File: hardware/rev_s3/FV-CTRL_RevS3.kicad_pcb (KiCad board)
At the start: 2 copper layers, 100 x 100 mm, 69 parts, among them J1 12V INPUT, J10 LIMIT SWITCHES, J11 DROP SENSOR COL 1, J12 DROP SENSOR COL 2, J2 XL4015 A, J21 USB_C_16P, J3 XL4015 B, J4 5V R-78E5.0-1.0, J5 S1_TOP, J6 S1_BOT, J7 S2_TOP, J8 S2_BOT, J9 I2C SPARE, SW1 RESET, SW2 BOOT, U1 ESP32-S3-WROOM-1U, U3 LD1117S33

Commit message: fix: reinforce RevS3 servo B supply route
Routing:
- net +6V_B: track 145.7 -> 223.0 mm
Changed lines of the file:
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@@
+	)
+	(segment
+		(start 198 175.54)
+		(end 198 185.54)
+		(width 1.2)
+		(layer "F.Cu")
+		(net "+6V_B")
 	)
 	(segment
@@
 	)
 	(segment
+		(start 198 185.54)
+		(end 194 185.54)
+		(width 1.2)
+		(layer "F.Cu")
+		(net "+6V_B")
+	)
+	(segment
 		(start 121.6 189.9)
 		(end 121.75 189.9)
@@
 	)
 	(segment
+		(start 198 175.54)
+		(end 194 175.54)
+		(width 1.2)
+		(layer "F.Cu")
+		(net "+6V_B")
+	)
+	(segment
 		(start 183.15 144.5)
 		(end 183.15 144.6)
@@
 	)
 	(segment
+		(start 198 126.2)
+		(end 198 175.54)
+		(width 1.2)
+		(layer "F.Cu")
+		(net "+6V_B")
+	)
+	(segment
 		(start 186.75 130.949999)
 		(end 186.7 131)
@@
 		(layer "F.Cu")
 		(net "+6V_B")
+	)
+	(segment
+		(start 188.1 126.2)
+		(end 198 126.2)
+		(width 1.2)
+		(layer "F.Cu")
+		(net "+6V_B")

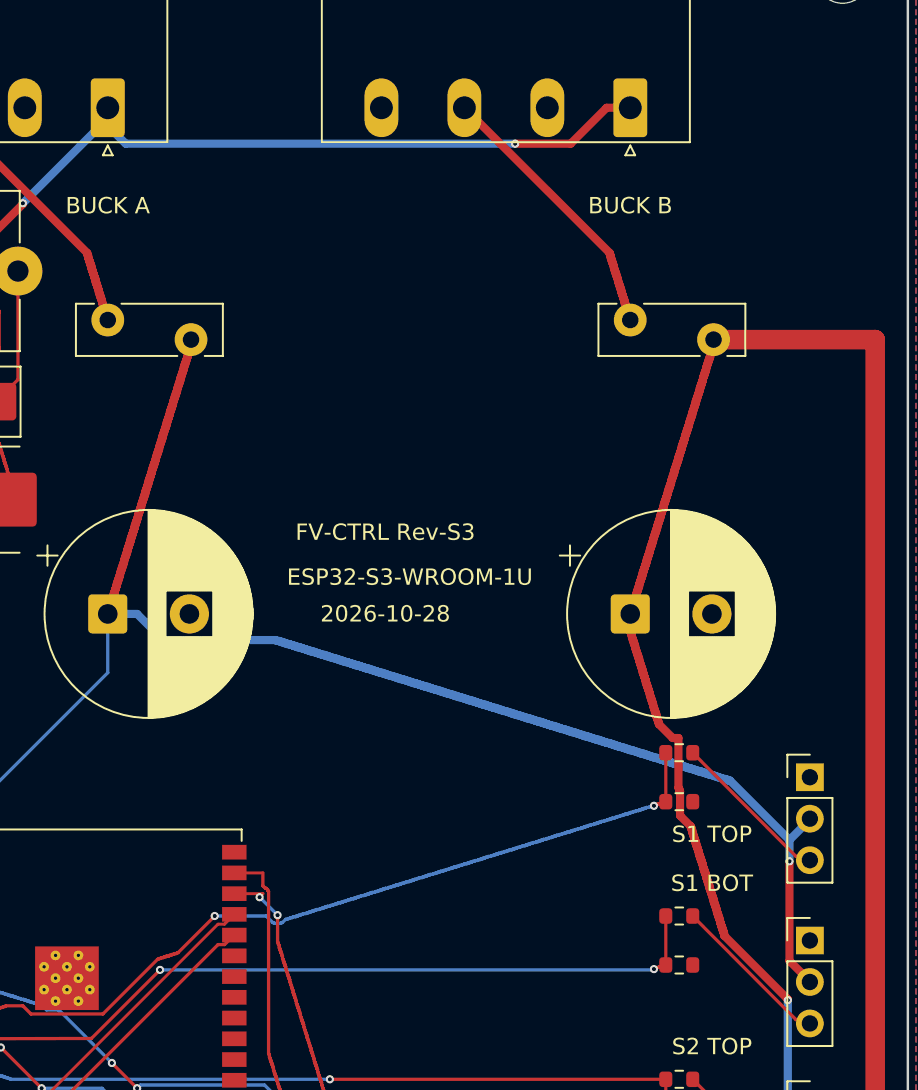
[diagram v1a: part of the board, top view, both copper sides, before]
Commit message: fix: reinforce RevS3 servo A and shared 12V routes
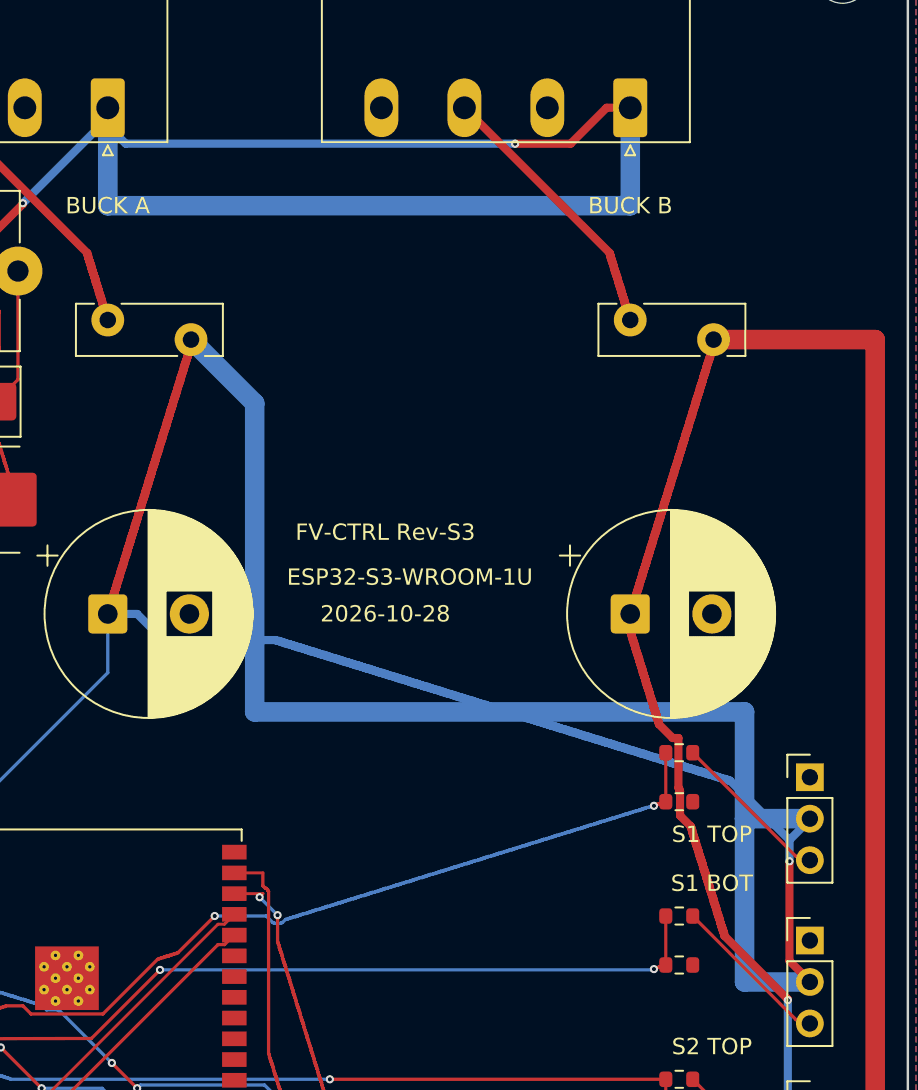
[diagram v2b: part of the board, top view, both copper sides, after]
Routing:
- net +6V_A: track 137.8 -> 216.8 mm
- net +12V: track 148.8 -> 192.8 mm
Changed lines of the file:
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@@
 	)
 	(segment
+		(start 151 118)
+		(end 183 118)
+		(width 1.2)
+		(layer "B.Cu")
+		(net "+12V")
+	)
+	(segment
+		(start 183 118)
+		(end 183 112)
+		(width 1.2)
+		(layer "B.Cu")
+		(net "+12V")
+	)
+	(segment
 		(start 119.6 145.75)
 		(end 117.2 143.35)
@@
 	)
 	(segment
+		(start 151 112)
+		(end 151 118)
+		(width 1.2)
+		(layer "B.Cu")
+		(net "+12V")
+	)
+	(segment
 		(start 145.8 117.85)
 		(end 150.7 112.95)
@@
 	)
 	(segment
+		(start 190 149)
+		(end 190 155.54)
+		(width 1.2)
+		(layer "B.Cu")
+		(net "+6V_A")
+	)
+	(segment
 		(start 168.25 146.75)
 		(end 168.15 146.75)
@@
 	)
 	(segment
+		(start 160 149)
+		(end 190 149)
+		(width 1.2)
+		(layer "B.Cu")
+		(net "+6V_A")
+	)
+	(segment
 		(start 162.15 144.85)
 		(end 162 144.85)
@@
 	)
 	(segment
+		(start 156.1 126.2)
+		(end 160 130.1)
+		(width 1.2)
+		(layer "B.Cu")
+		(net "+6V_A")
+	)
+	(segment
 		(start 186.1 152.3)
 		(end 186.05 152.25)
@@
 	)
 	(segment
+		(start 160 130.1)
+		(end 160 149)
+		(width 1.2)
+		(layer "B.Cu")
+		(net "+6V_A")
+	)
+	(segment
 		(start 167 146.35)
 		(end 166.85 146.35)
@@
 	)
 	(segment
+		(start 190 155.54)
+		(end 190 165.54)
+		(width 1.2)
+		(layer "B.Cu")
+		(net "+6V_A")
+	)
+	(segment
 		(start 181.7 150.9)
 		(end 181.55 150.9)
@@
 	)
 	(segment
+		(start 190 155.54)
+		(end 194 155.54)
+		(width 1.2)
+		(layer "B.Cu")
+		(net "+6V_A")
+	)
+	(segment
 		(start 169.4 147.1)
 		(end 169.3 147.1)
@@
 		(layer "B.Cu")
 		(net "+6V_A")
+	)
+	(segment
+		(start 190 165.54)
+		(end 194 165.54)
+		(width 1.2)
+		(layer "B.Cu")
+		(net "+6V_A")

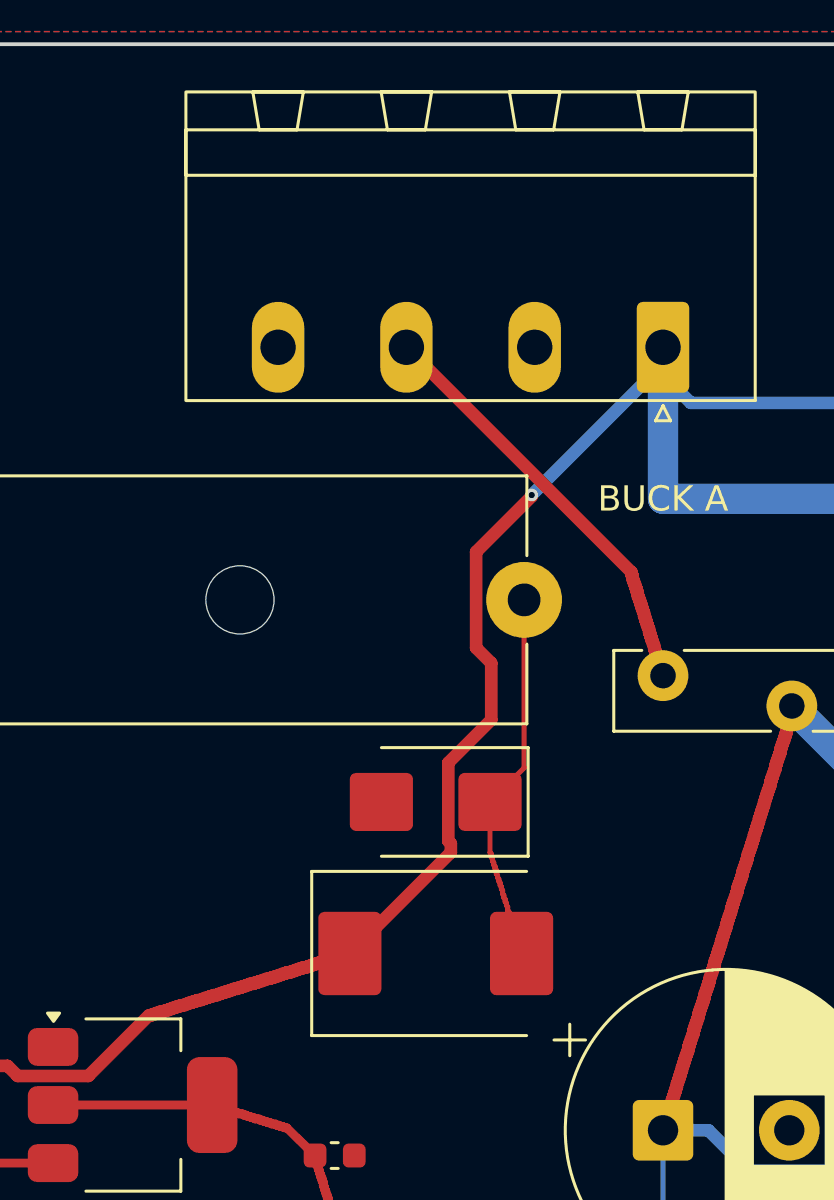
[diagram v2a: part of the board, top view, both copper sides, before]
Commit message: fix: improve RevS3 12V input path and schematic parity
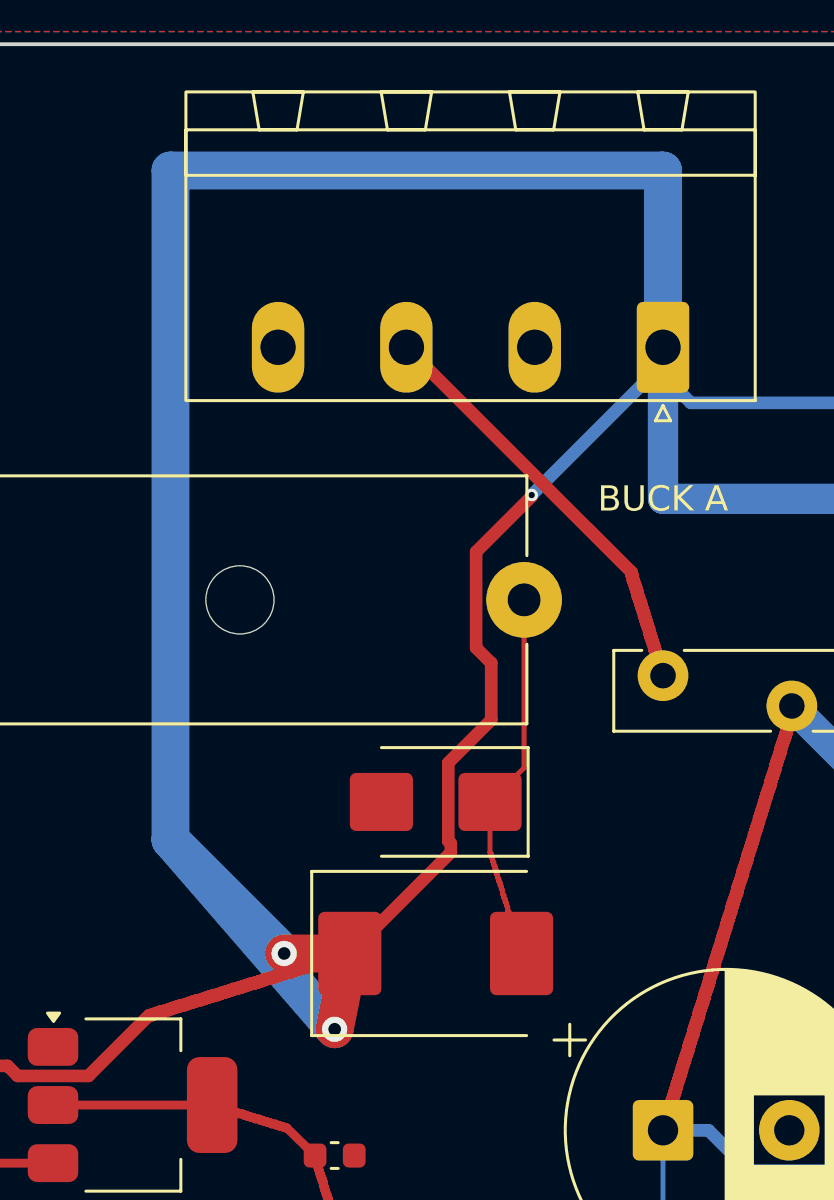
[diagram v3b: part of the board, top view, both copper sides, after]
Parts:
- C1, C2: footprint CP_Radial_D12.5mm_P5.00mm -> Capacitor_THT:CP_Radial_D12.5mm_P5.00mm
- C10, C58, C6: footprint C_0603_1608Metric -> Capacitor_SMD:C_0603_1608Metric
- C57: footprint CP_Radial_D5.0mm_P2.00mm -> Capacitor_THT:CP_Radial_D5.0mm_P2.00mm
- D1: footprint D_SMB -> Diode_SMD:D_SMB
- D2, D3, D4, D5, D6: footprint LED_0603_1608Metric -> LED_SMD:LED_0603_1608Metric
- D7: footprint D_SMC -> Diode_SMD:D_SMC
- F1: footprint Fuseholder_Cylinder-5x20mm_Schurter_0031_8201_Horizontal_Open -> Fuse:Fuseholder_Cylinder-5x20mm_Schurter_0031_8201_Horizontal_Open
- F2, F3: footprint Fuse_Bourns_MF-RHT300 -> Fuse:Fuse_Bourns_MF-RHT300
- J1: footprint PhoenixContact_MSTBA_2,5_2-G-5,08_1x02_P5.08mm_Horizontal -> Connector_Phoenix_MSTB:PhoenixContact_MSTBA_2,5_2-G-5,08_1x02_P5.08mm_Horizontal
- J10, J9: footprint PinHeader_1x04_P2.54mm_Vertical -> Connector_PinHeader_2.54mm:PinHeader_1x04_P2.54mm_Vertical
- J11, J12: footprint JST_XH_B4B-XH-A_1x04_P2.50mm_Vertical -> Connector_JST:JST_XH_B4B-XH-A_1x04_P2.50mm_Vertical
- J2, J3: footprint PhoenixContact_MSTBA_2,5_4-G-5,08_1x04_P5.08mm_Horizontal -> Connector_Phoenix_MSTB:PhoenixContact_MSTBA_2,5_4-G-5,08_1x04_P5.08mm_Horizontal
- J21: footprint USB_C_Receptacle_GCT_USB4105-xx-A_16P_TopMnt_Horizontal -> Connector_USB:USB_C_Receptacle_GCT_USB4105-xx-A_16P_TopMnt_Horizontal
- J4: footprint RECOM_R78E5V1A -> fv_modules:RECOM_R78E5V1A
- J5, J6, J7, J8: footprint PinHeader_1x03_P2.54mm_Vertical -> Connector_PinHeader_2.54mm:PinHeader_1x03_P2.54mm_Vertical
- R1, R10, R11, R12, R14, R15, R16, R17, R18, R19, R2, R21, R22, R23, R24, R25, R26, R27, R3, R4, R5, R6, R7, R8: footprint R_0603_1608Metric -> Resistor_SMD:R_0603_1608Metric
- SW1, SW2: footprint SW_Push_SPST_NO_Alps_SKRK -> Button_Switch_SMD:SW_Push_SPST_NO_Alps_SKRK
- TP1, TP2, TP3, TP4, TP5, TP6, TP7, TP8: footprint TestPoint_Pad_D1.5mm -> TestPoint:TestPoint_Pad_D1.5mm
- U1: footprint ESP32-S3-WROOM-1U -> RF_Module:ESP32-S3-WROOM-1U
- U3: footprint SOT-223-3_TabPin2 -> Package_TO_SOT_SMD:SOT-223-3_TabPin2
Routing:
- net +12V: track 192.8 -> 267.7 mm, vias 3 -> 5

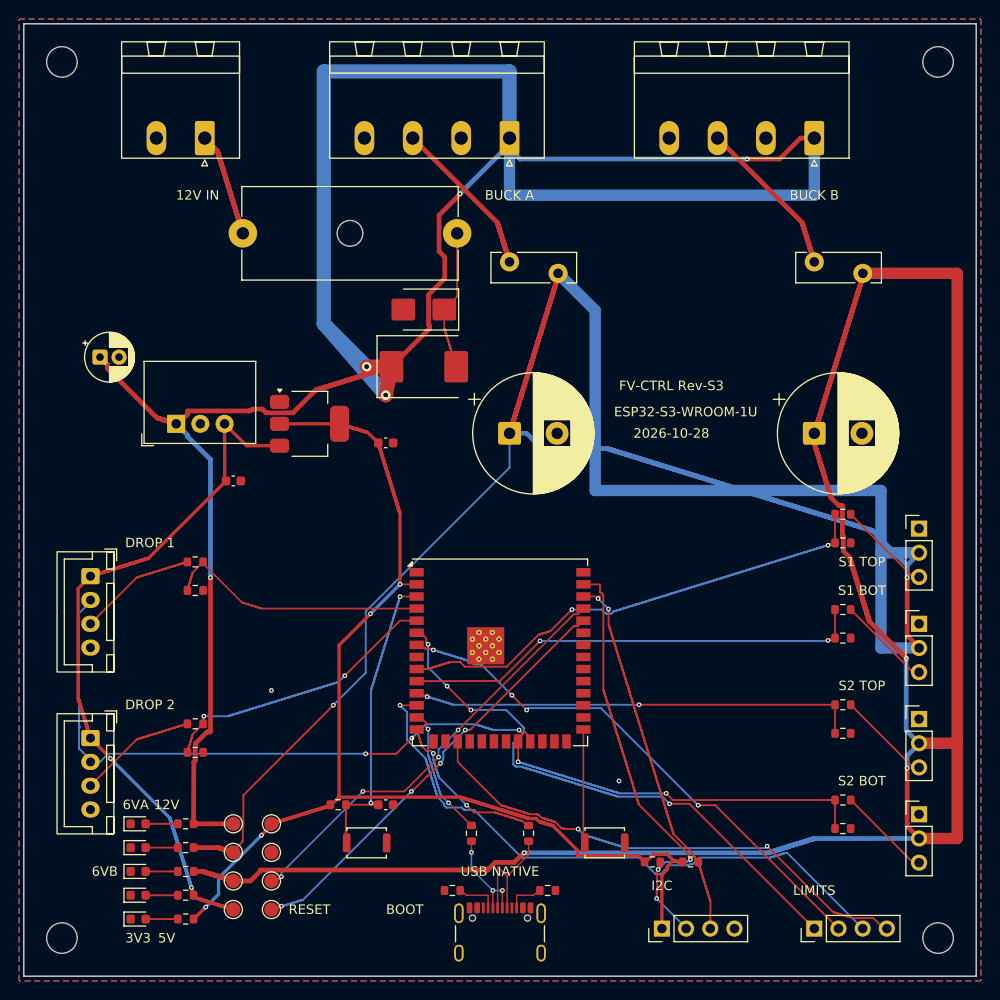
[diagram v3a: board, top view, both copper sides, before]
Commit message: fix: raise Rev-S3 minimum drill to 0.3 mm
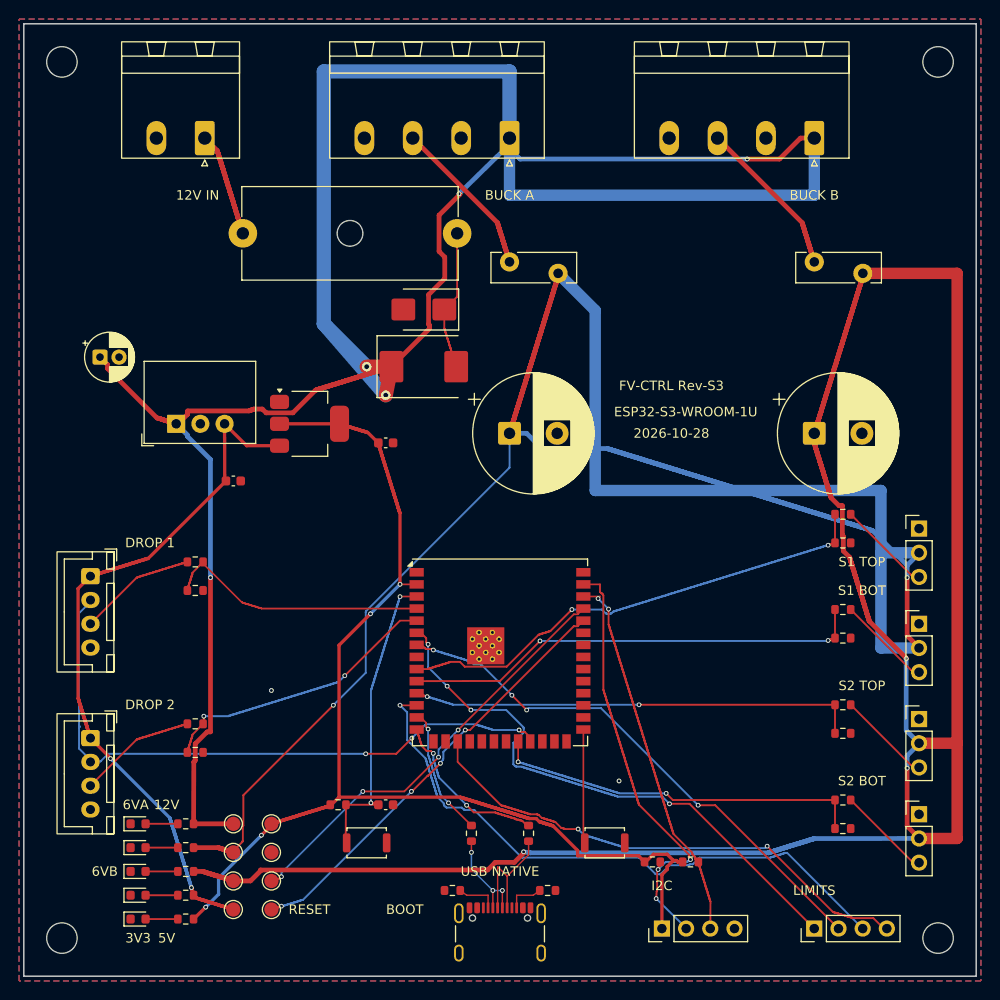
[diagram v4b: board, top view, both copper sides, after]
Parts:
- U1: footprint RF_Module:ESP32-S3-WROOM-1U -> fv_rev_s3:ESP32-S3-WROOM-1U_0p3

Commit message: fix: align Rev-S3 USB-C VBUS schematic parity
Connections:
- net Net-(J21-VBUS_L) renamed USB_VBUS_UNUSED_L
- net Net-(J21-VBUS_R) renamed USB_VBUS_UNUSED_R
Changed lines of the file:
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@@
 			(layers "F.Cu" "F.Mask" "F.Paste")
 			(roundrect_rratio 0.25)
-			(net "Net-(J21-VBUS_L)")
+			(net "USB_VBUS_UNUSED_L")
 		)
 		(pad "A5" smd roundrect
@@
 			(layers "F.Cu" "F.Mask" "F.Paste")
 			(roundrect_rratio 0.25)
-			(net "Net-(J21-VBUS_R)")
+			(net "USB_VBUS_UNUSED_R")
 		)
 		(pad "A12" smd roundrect
@@
 			(layers "F.Cu" "F.Mask" "F.Paste")
 			(roundrect_rratio 0.25)
-			(net "Net-(J21-VBUS_R)")
+			(net "USB_VBUS_UNUSED_R")
 		)
 		(pad "B5" smd roundrect
@@
 			(layers "F.Cu" "F.Mask" "F.Paste")
 			(roundrect_rratio 0.25)
-			(net "Net-(J21-VBUS_L)")
+			(net "USB_VBUS_UNUSED_L")
 		)
 		(pad "B12" smd roundrect
